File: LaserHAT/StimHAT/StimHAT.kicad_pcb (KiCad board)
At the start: 4 copper layers, 65 x 57 mm, 112 parts, among them J1 GPIO, J10 OLED 0.91 (GND VCC SCL SDA), J101 ELECTRODE E1/E2, J102 B4B-PH-K-S(LF)(SN), J103 5V TO DC-DC POD, J5 GT-USB-7010ASV, J6 BNC TRIGGER IN, J7 BNC STIM OUT, Q3 AP30P30Q, Q4 DMMT5401, Q5 AP30P30Q, SW10 MSK12C02, SW6 TS-1088-AR02016, SW7 SKRHADE010, SW9 TS-1088-AR02016, U1 M24C32-WDW6TP, U101 ISO7741FDBQR, U104 TLV76050DBZR, U105 DAC60501ZDGSR, U106 OPA2192IDGKR, U107 CD74HC4053PWR, U108 DG418DY-T1-E3, U109 ISO1640BDR, U110 TLV1702AIDGKR, U4 MCP1700T-3302E/MB, U5 AP2171W, U6 CH340N, U7 MSPM0G1507SRHBR, U8 74LVC2G17GW

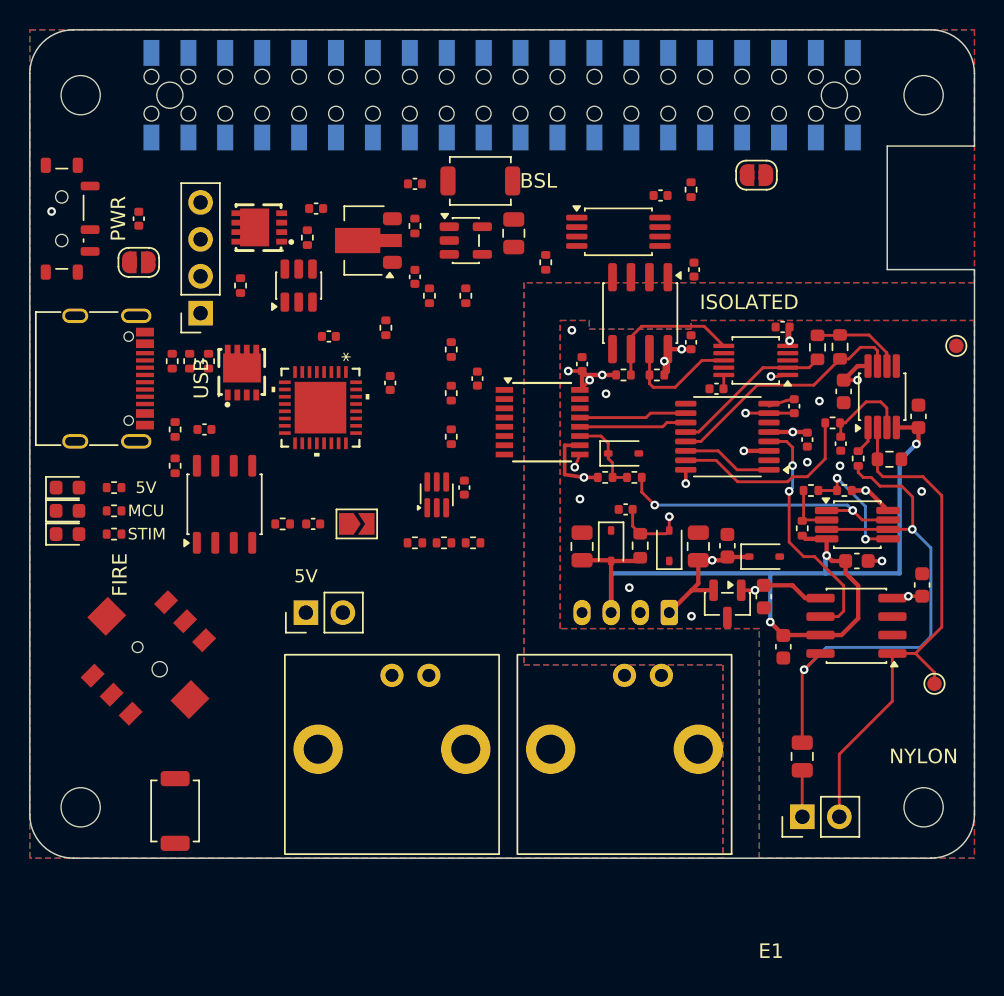
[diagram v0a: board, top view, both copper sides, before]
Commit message: StimHAT: USB-C power / switch / CH340 corner regrouped and hand-routed
After the user's isolated-block clean-up: C118's position synced into place.py, U105.1's +5V_ISO
stub re-added, two dangling +V_STIM leftovers (and their via) removed.

West corner: Q5 (VBUS switch), Q3 (ideal-diode P-FET) and Q4 (DMMT5401) in one column east of
J10, R21 / R22 / R26 / C12 beside them, R8 / R10 straight off the CC pads, C17 and JP4 east of U6,
R19 / R20 north of J10, R4 / C1 north of U7.  Routed by hand: VBUS (both pad pairs), PWR_EN to
SW10 (In2), VBUS_SW bridge and sense, +5V to C12 / Q4 / U4.2, IDEAL_G / IDEAL_B, CC1 / CC2,
USB D+/D- into U6 (D+ pair tied through vias under the jack).  The corridor from U7.14/15 to
U6.7/6 is left free for the UART lines.  DRC 0 errors / 0 warnings, 96 open connections.

Co-Authored-By: Claude Fable 5.1 <noreply@anthropic.com>
Claude-Session: https://claude.ai/code/session_015kiXLxnPpBaXdXJu2EMvn7
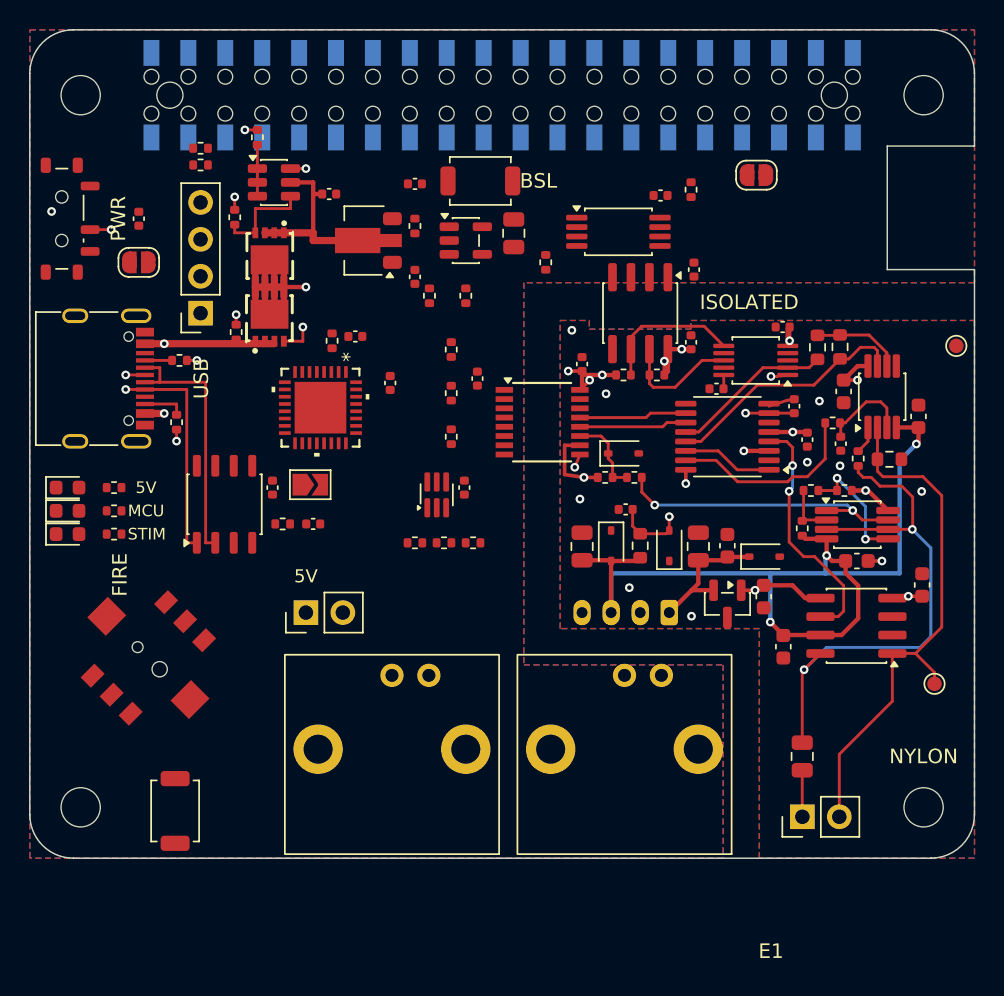
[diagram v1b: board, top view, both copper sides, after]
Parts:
- moved R20 14.7 mm to (11.8, 8.15), turned to 0 degrees
- moved R4 13.8 mm to (20.8, 21.4)
- moved R19 13.5 mm to (11.8, 9.30), turned to 0 degrees
- moved R22 12.9 mm to (14.1, 12.9)
- moved Q3 8.32 mm to (16.5, 15.5), turned to 180 degrees
- moved R21 7.71 mm to (15.7, 7.40)
- moved Q4 7.30 mm to (16.8, 10.5), turned to 0 degrees
- moved Q5 6.34 mm to (16.5, 19.9), turned to 0 degrees
- moved C17 6.16 mm to (16.7, 31.5), turned to -90 degrees
- moved JP4 4.19 mm to (19.3, 31.3)
- moved R26 3.21 mm to (14.2, 20.8)
- moved C1 1.82 mm to (22.4, 21.1)
- moved C12 1.35 mm to (20.6, 11.3)
- moved R10 0.51 mm to (10.1, 27.0), turned to -90 degrees
- moved R8 0.50 mm to (10.3, 22.8), turned to 0 degrees
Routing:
- net /PWR_EN: track 0.00 -> 26.1 mm, vias 0 -> 3
- net VBUS_SW: track 0.00 -> 18.0 mm, vias 0 -> 2
- net USB_DM: track 0.00 -> 17.9 mm
- net USB_DP: track 0.00 -> 17.8 mm, vias 0 -> 2
- net VBUS: track 0.00 -> 15.0 mm, vias 0 -> 2
- net +5V: track 0.00 -> 14.9 mm
- net /IDEAL_G: track 0.00 -> 6.92 mm
- net /IDEAL_B: track 0.00 -> 3.54 mm
- net GND: track 0.00 -> 3.23 mm, vias 1 -> 5
- net Net-(J5-CC2): track 0.00 -> 2.92 mm
- net +V_STIM: track 54.1 -> 52.2 mm, vias 5 -> 4
- net Net-(J5-CC1): track 0.00 -> 1.87 mm
- net +5V_ISO: track 81.7 -> 82.9 mm
